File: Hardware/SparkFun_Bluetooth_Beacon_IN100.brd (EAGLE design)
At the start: 25.4 x 25.4 mm, 43 parts, among them J3 Vertical Qwiic Connector, U1 IN100, Y1 CRYSTAL-26MHZSMD-3.2X2.5

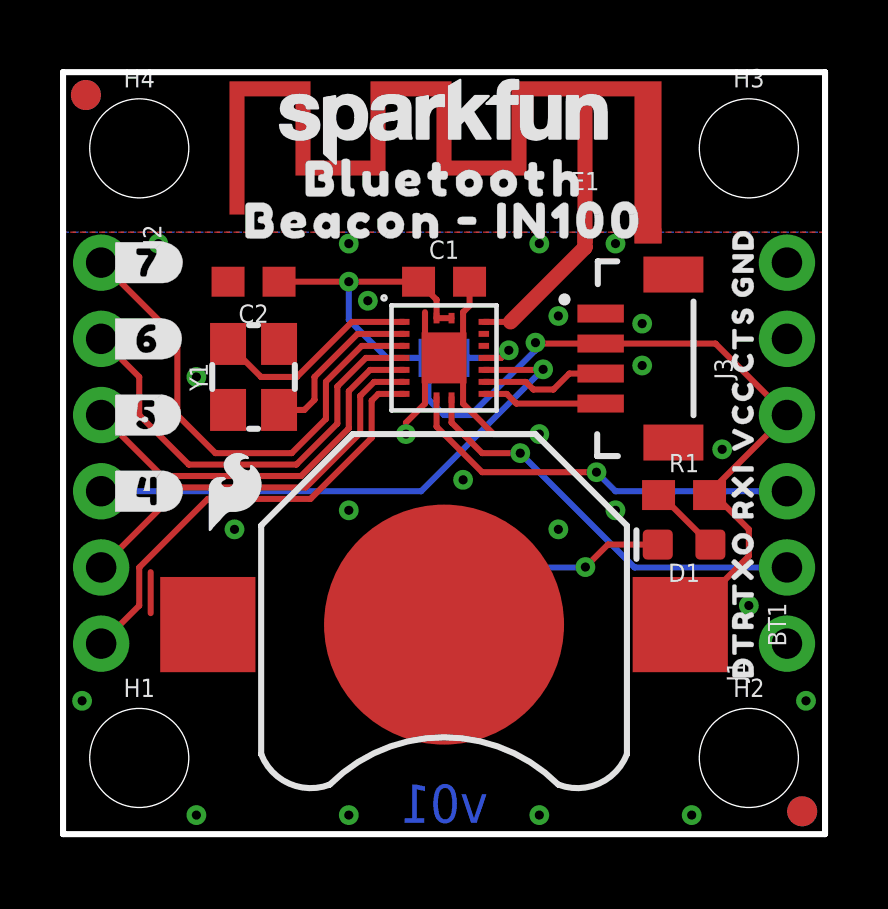
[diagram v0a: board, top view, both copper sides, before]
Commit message: Pre-review cleanup
Clean up schematic
Add "programmed" checkbox to bottom silk
Add SW0 and SW1 to top silk
Update measures
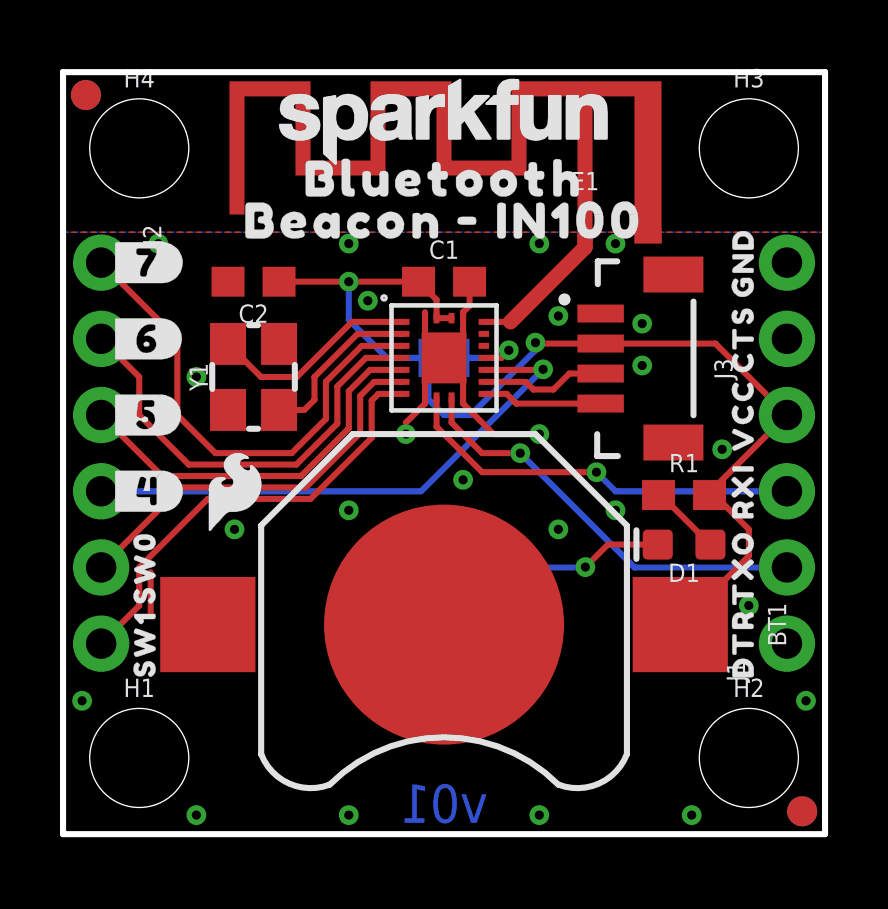
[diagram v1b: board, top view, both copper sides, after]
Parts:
- added U$20: (no value), output:#PROGRAMMED#0
- added U$21: (no value), output:SW00
- added U$22: (no value), output:SW10
- moved FRAME1 8.52 mm to (-10.2, -21.6)
- moved LOGO1 7.62 mm to (12.7, 11.4)
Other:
- board text added: "Dryw Wade"
- board text added: "Units: inches"
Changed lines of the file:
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@@
 </polygon>
 <text x="12.7" y="1.016" size="1.27" layer="16" font="vector" ratio="15" rot="SMR0" align="center">v01</text>
-<dimension x1="0" y1="0" x2="25.4" y2="0" x3="12.7" y3="-3.81" textsize="1.778" textratio="15" layer="47" unit="inch"/>
-<dimension x1="0" y1="0" x2="0" y2="25.4" x3="-1.27" y3="12.7" textsize="1.778" textratio="15" layer="47" unit="inch"/>
+<wire x1="7.62" y1="4.4196" x2="6.35" y2="4.4196" width="0.1524" layer="22"/>
+<wire x1="6.35" y1="4.4196" x2="6.35" y2="3.2004" width="0.1524" layer="22"/>
+<wire x1="6.35" y1="3.2004" x2="7.62" y2="3.2004" width="0.1524" layer="22"/>
+<text x="16.51" y="-21.59" size="1.778" layer="51">Dryw Wade</text>
+<dimension x1="0" y1="0" x2="2.54" y2="0" x3="1.27" y3="-3.81" textsize="1.778" textratio="15" layer="47" unit="inch"/>
+<dimension x1="0" y1="0" x2="22.86" y2="0" x3="11.43" y3="-7.62" textsize="1.778" textratio="15" layer="47" unit="inch"/>
+<dimension x1="0" y1="0" x2="25.4" y2="0" x3="12.7" y3="-11.43" textsize="1.778" textratio="15" layer="47" unit="inch"/>
+<dimension x1="0" y1="0" x2="0" y2="6.35" x3="-1.27" y3="3.175" textsize="1.778" textratio="15" layer="47" unit="inch"/>
+<dimension x1="0" y1="0" x2="0" y2="2.54" x3="-5.08" y3="1.27" textsize="1.778" textratio="15" layer="47" unit="inch"/>
+<dimension x1="0" y1="0" x2="0" y2="19.05" x3="-8.89" y3="9.525" textsize="1.778" textratio="15" layer="47" unit="inch"/>
+<dimension x1="0" y1="0" x2="0" y2="22.86" x3="-12.7" y3="11.43" textsize="1.778" textratio="15" layer="47" unit="inch"/>
+<dimension x1="0" y1="0" x2="0" y2="25.4" x3="-16.51" y3="12.7" textsize="1.778" textratio="15" layer="47" unit="inch"/>
+<text x="-15.24" y="-7.62" size="1.778" layer="47" font="vector" ratio="15">Units: inches</text>
 </plain>
 <attributes>
@@
 <attribute name="VALUE" x="17.399" y="21.209" size="0.6096" layer="27" font="vector" ratio="20" align="top-center"/>
 </element>
-<element name="FRAME1" library="SparkFun-Aesthetics" package="CREATIVE_COMMONS" value="FRAME-LETTER" x="-13.97" y="-13.97" smashed="yes">
-<attribute name="DESIGNER" value="" x="-13.97" y="-13.97" size="1.778" layer="27" font="vector" ratio="15" display="off"/>
-<attribute name="REV" value="" x="-13.97" y="-13.97" size="1.778" layer="27" font="vector" ratio="15" display="off"/>
+<element name="FRAME1" library="SparkFun-Aesthetics" package="CREATIVE_COMMONS" value="FRAME-LETTER" x="-10.16" y="-21.59" smashed="yes">
+<attribute name="DESIGNER" value="" x="-10.16" y="-21.59" size="1.778" layer="27" font="vector" ratio="15" display="off"/>
+<attribute name="REV" value="" x="-10.16" y="-21.59" size="1.778" layer="27" font="vector" ratio="15" display="off"/>
 </element>
 <element name="U1" library="IN100" package="IN100" value="IN100" x="12.7" y="15.875" smashed="yes"/>
@@
 <element name="U$7" library="output" package="#_4#0" value="" x="1.397" y="11.43" smashed="yes"/>
 <element name="U$8" library="SparkFun-Aesthetics" package="SFE_LOGO_FLAME_.1" value="" x="5.715" y="11.43" smashed="yes"/>
-<element name="LOGO1" library="SparkFun-Aesthetics" package="OSHW-LOGO-S" value="OSHW-LOGOS" x="12.7" y="3.81" smashed="yes" rot="MR0"/>
+<element name="LOGO1" library="SparkFun-Aesthetics" package="OSHW-LOGO-S" value="OSHW-LOGOS" x="12.7" y="11.43" smashed="yes" rot="MR0"/>
 <element name="LOGO2" library="SparkFun-Aesthetics" package="SFE_LOGO_NAME_FLAME_.1" value="SFE_LOGO_NAME_FLAME.1_INCH" x="12.7" y="21.59" smashed="yes" rot="MR0"/>
 <element name="U$9" library="output" package="BLUETOOTH0" value="" x="12.7" y="19.304" smashed="yes" rot="MR0"/>
@@
 </element>
 <element name="U$19" library="output" package="#PWR#0" value="" x="12.7" y="7.239" smashed="yes" rot="MR0"/>
+<element name="U$20" library="output" package="#PROGRAMMED#0" value="" x="7.239" y="3.81" smashed="yes" rot="MR0"/>
+<element name="U$21" library="output" package="SW00" value="" x="2.7305" y="8.89" smashed="yes" rot="R90"/>
+<element name="U$22" library="output" package="SW10" value="" x="2.7305" y="6.35" smashed="yes" rot="R90"/>
 </elements>
 <signals>

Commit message: Design review updates
Add TX/RX labels to IN100 symbol
Add text to jumpers in schematic
Add VCC range to schematic
Rename PWR jumper in schematic
Increase crystal trace width to 10mil
Add more GND vias near RF trace
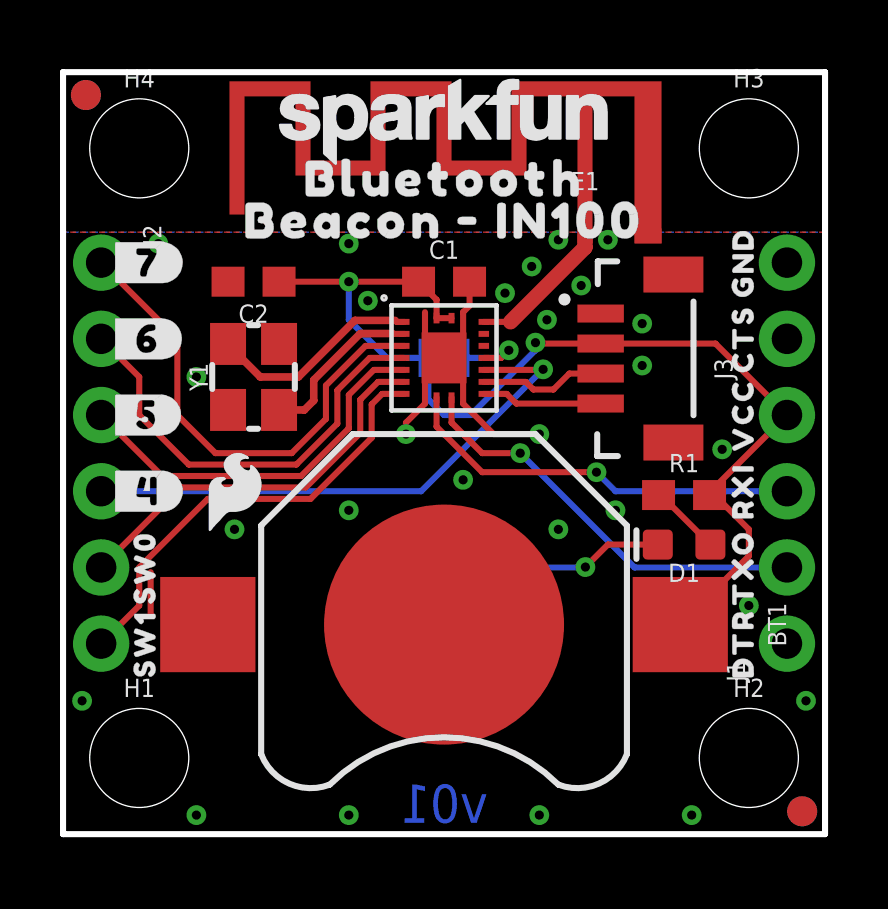
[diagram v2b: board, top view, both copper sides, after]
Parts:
- renumbered VDDQ1 to PWR
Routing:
- net GND: vias 24 -> 27
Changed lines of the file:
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@@
 <drawing>
 <settings>
-<setting alwaysvectorfont="yes"/>
+<setting alwaysvectorfont="no"/>
 <setting verticaltext="up"/>
 </settings>
@@
 <attribute name="VALUE" x="20.701" y="10.541" size="0.6096" layer="27" font="vector" ratio="20" align="top-center"/>
 </element>
-<element name="VDDQ1" library="SparkFun-Jumpers" package="SMT-JUMPER_2_NC_TRACE_SILK" package3d_urn="urn:adsk.eagle:package:39281/1" value="JUMPER-SMT_2_NC_TRACE_SILK" x="12.7" y="8.89" smashed="yes" rot="MR180">
+<element name="PWR" library="SparkFun-Jumpers" package="SMT-JUMPER_2_NC_TRACE_SILK" package3d_urn="urn:adsk.eagle:package:39281/1" value="JUMPER-SMT_2_NC_TRACE_SILK" x="12.7" y="8.89" smashed="yes" rot="MR180">
 <attribute name="NAME" x="12.7" y="7.747" size="0.6096" layer="26" font="vector" ratio="20" rot="MR180" align="bottom-center"/>
 <attribute name="VALUE" x="12.7" y="10.033" size="0.6096" layer="28" font="vector" ratio="20" rot="MR180" align="top-center"/>
@@
 <wire x1="13.55" y1="17.614" x2="13.335" y2="17.399" width="0.2032" layer="1"/>
 <via x="3.175" y="19.685" extent="1-16" drill="0.3048"/>
-<via x="15.875" y="19.685" extent="1-16" drill="0.3048"/>
+<via x="16.51" y="19.812" extent="1-16" drill="0.3048"/>
 <via x="9.525" y="19.685" extent="1-16" drill="0.3048"/>
-<via x="16.51" y="17.272" extent="1-16" drill="0.3048"/>
+<via x="16.129" y="17.145" extent="1-16" drill="0.3048"/>
 <via x="15.875" y="13.335" extent="1-16" drill="0.3048"/>
 <via x="21.971" y="12.827" extent="1-16" drill="0.3048"/>
@@
 <via x="22.86" y="7.62" extent="1-16" drill="0.3048"/>
 <via x="19.304" y="15.621" extent="1-16" drill="0.3048"/>
-<via x="18.415" y="19.685" extent="1-16" drill="0.3048"/>
+<via x="18.161" y="19.812" extent="1-16" drill="0.3048"/>
 <wire x1="11.43" y1="13.335" x2="11.43" y2="13.716" width="0.2032" layer="1"/>
 <wire x1="11.43" y1="13.716" x2="12.065" y2="14.351" width="0.2032" layer="1"/>
 <wire x1="15.875" y1="13.335" x2="14.351" y2="13.335" width="0.2032" layer="1"/>
 <wire x1="14.351" y1="13.335" x2="13.335" y2="14.351" width="0.2032" layer="1"/>
-<contactref element="VDDQ1" pad="1"/>
+<contactref element="PWR" pad="1"/>
 <via x="16.51" y="10.16" extent="1-16" drill="0.3048"/>
 <via x="19.304" y="17.018" extent="1-16" drill="0.3048"/>
@@
 <via x="13.335" y="11.811" extent="1-16" drill="0.3048"/>
 <via x="9.525" y="10.795" extent="1-16" drill="0.3048"/>
+<via x="14.732" y="18.034" extent="1-16" drill="0.3048"/>
+<via x="17.272" y="18.288" extent="1-16" drill="0.3048"/>
+<via x="15.621" y="18.923" extent="1-16" drill="0.3048"/>
 </signal>
 <signal name="N$4">
@@
 <contactref element="U1" pad="1"/>
 <contactref element="Y1" pad="3"/>
-<wire x1="5.5" y1="16.34" x2="6.6" y2="15.24" width="0.2032" layer="1"/>
-<wire x1="9.63013125" y1="17.075" x2="11.375" y2="17.075" width="0.2032" layer="1"/>
-<wire x1="7.79513125" y1="15.24" x2="9.63013125" y2="17.075" width="0.2032" layer="1"/>
-<wire x1="6.6" y1="15.24" x2="7.79513125" y2="15.24" width="0.2032" layer="1"/>
+<wire x1="6.5746" y1="15.24" x2="5.5" y2="16.3146" width="0.254" layer="1"/>
+<wire x1="5.5" y1="16.34" x2="5.5" y2="16.3146" width="0.254" layer="1"/>
+<wire x1="11.121" y1="17.075" x2="11.375" y2="17.075" width="0.2032" layer="1"/>
+<wire x1="11.121" y1="17.075" x2="11.0702" y2="17.1258" width="0.2032" layer="1"/>
+<wire x1="11.0702" y1="17.1258" x2="9.73173125" y2="17.1258" width="0.254" layer="1"/>
+<wire x1="7.84593125" y1="15.24" x2="9.73173125" y2="17.1258" width="0.254" layer="1"/>
+<wire x1="6.5746" y1="15.24" x2="7.84593125" y2="15.24" width="0.254" layer="1"/>
 </signal>
 <signal name="N$2">
 <contactref element="U1" pad="2"/>
 <contactref element="Y1" pad="1"/>
-<wire x1="11.375" y1="16.675" x2="9.817" y2="16.675" width="0.2032" layer="1"/>
-<wire x1="9.817" y1="16.675" x2="8.382" y2="15.24" width="0.2032" layer="1"/>
-<wire x1="8.382" y1="15.24" x2="8.382" y2="14.478" width="0.2032" layer="1"/>
-<wire x1="8.382" y1="14.478" x2="8.044" y2="14.14" width="0.2032" layer="1"/>
-<wire x1="8.044" y1="14.14" x2="7.2" y2="14.14" width="0.2032" layer="1"/>
+<wire x1="11.375" y1="16.675" x2="10.994" y2="16.675" width="0.2032" layer="1"/>
+<wire x1="10.994" y1="16.675" x2="10.9813" y2="16.6877" width="0.2032" layer="1"/>
+<wire x1="10.9813" y1="16.6877" x2="9.9059" y2="16.6877" width="0.254" layer="1"/>
+<wire x1="9.9059" y1="16.6877" x2="8.3566" y2="15.1384" width="0.254" layer="1"/>
+<wire x1="8.3566" y1="15.1384" x2="8.3566" y2="14.4526" width="0.254" layer="1"/>
+<wire x1="8.3566" y1="14.4526" x2="8.044" y2="14.14" width="0.254" layer="1"/>
+<wire x1="8.044" y1="14.14" x2="7.2" y2="14.14" width="0.254" layer="1"/>
 </signal>
 <signal name="VCC">
@@
 <signal name="SW0">
 <contactref element="U1" pad="6"/>
-<wire x1="11.375" y1="15.075" x2="10.372275" y2="15.075" width="0.2032" layer="1"/>
-<wire x1="10.372275" y1="15.075" x2="9.906" y2="14.608725" width="0.2032" layer="1"/>
+<wire x1="11.375" y1="15.075" x2="10.499275" y2="15.075" width="0.2032" layer="1"/>
+<wire x1="10.499275" y1="15.075" x2="9.906" y2="14.481725" width="0.2032" layer="1"/>
 <wire x1="9.906" y1="13.36954375" x2="8.09345625" y2="11.557" width="0.2032" layer="1"/>
-<wire x1="9.906" y1="14.608725" x2="9.906" y2="13.36954375" width="0.2032" layer="1"/>
+<wire x1="9.906" y1="14.481725" x2="9.906" y2="13.36954375" width="0.2032" layer="1"/>
 <wire x1="8.09345625" y1="11.557" x2="3.937" y2="11.557" width="0.2032" layer="1"/>
 <contactref element="J2" pad="5"/>
@@
 <signal name="SW1">
 <contactref element="U1" pad="7"/>
-<wire x1="11.375" y1="14.675" x2="10.51109375" y2="14.675" width="0.2032" layer="1"/>
-<wire x1="10.287" y1="14.45090625" x2="10.287" y2="13.211725" width="0.2032" layer="1"/>
-<wire x1="10.51109375" y1="14.675" x2="10.287" y2="14.45090625" width="0.2032" layer="1"/>
+<wire x1="11.375" y1="14.675" x2="10.63809375" y2="14.675" width="0.2032" layer="1"/>
+<wire x1="10.287" y1="14.32390625" x2="10.287" y2="13.211725" width="0.2032" layer="1"/>
+<wire x1="10.63809375" y1="14.675" x2="10.287" y2="14.32390625" width="0.2032" layer="1"/>
 <wire x1="10.287" y1="13.211725" x2="8.251275" y2="11.176" width="0.2032" layer="1"/>
 <wire x1="4.826" y1="11.176" x2="2.54" y2="8.89" width="0.2032" layer="1"/>
@@
 <signal name="IO5">
 <contactref element="U1" pad="5"/>
-<wire x1="11.375" y1="15.475" x2="10.23345625" y2="15.475" width="0.2032" layer="1"/>
-<wire x1="10.23345625" y1="15.475" x2="9.525" y2="14.76654375" width="0.2032" layer="1"/>
+<wire x1="11.375" y1="15.475" x2="10.36045625" y2="15.475" width="0.2032" layer="1"/>
+<wire x1="10.36045625" y1="15.475" x2="9.525" y2="14.63954375" width="0.2032" layer="1"/>
 <wire x1="9.525" y1="13.5273625" x2="7.9356375" y2="11.938" width="0.2032" layer="1"/>
-<wire x1="9.525" y1="14.76654375" x2="9.525" y2="13.5273625" width="0.2032" layer="1"/>
+<wire x1="9.525" y1="14.63954375" x2="9.525" y2="13.5273625" width="0.2032" layer="1"/>
 <wire x1="3.302" y1="11.938" x2="7.9356375" y2="11.938" width="0.2032" layer="1"/>
 <contactref element="J2" pad="3"/>
@@
 <signal name="IO6">
 <contactref element="U1" pad="4"/>
-<wire x1="11.375" y1="15.875" x2="10.0946375" y2="15.875" width="0.2032" layer="1"/>
-<wire x1="10.0946375" y1="15.875" x2="9.144" y2="14.9243625" width="0.2032" layer="1"/>
+<wire x1="11.375" y1="15.875" x2="10.2216375" y2="15.875" width="0.2032" layer="1"/>
+<wire x1="10.2216375" y1="15.875" x2="9.144" y2="14.7973625" width="0.2032" layer="1"/>
 <wire x1="9.144" y1="13.68518125" x2="7.77781875" y2="12.319" width="0.2032" layer="1"/>
-<wire x1="9.144" y1="14.9243625" x2="9.144" y2="13.68518125" width="0.2032" layer="1"/>
+<wire x1="9.144" y1="14.7973625" x2="9.144" y2="13.68518125" width="0.2032" layer="1"/>
 <wire x1="2.54" y1="13.97" x2="2.54" y2="15.24" width="0.2032" layer="1"/>
 <wire x1="7.77781875" y1="12.319" x2="4.191" y2="12.319" width="0.2032" layer="1"/>
@@
 <signal name="IO7">
 <contactref element="U1" pad="3"/>
-<wire x1="11.375" y1="16.275" x2="9.95581875" y2="16.275" width="0.2032" layer="1"/>
-<wire x1="9.95581875" y1="16.275" x2="8.763" y2="15.08218125" width="0.2032" layer="1"/>
+<wire x1="11.375" y1="16.275" x2="10.08281875" y2="16.275" width="0.2032" layer="1"/>
+<wire x1="10.08281875" y1="16.275" x2="8.763" y2="14.95518125" width="0.2032" layer="1"/>
 <wire x1="8.763" y1="13.843" x2="7.62" y2="12.7" width="0.2032" layer="1"/>
-<wire x1="8.763" y1="15.08218125" x2="8.763" y2="13.843" width="0.2032" layer="1"/>
+<wire x1="8.763" y1="14.95518125" x2="8.763" y2="13.843" width="0.2032" layer="1"/>
 <wire x1="5.08" y1="12.7" x2="3.81" y2="13.97" width="0.2032" layer="1"/>
 <wire x1="3.81" y1="13.97" x2="3.81" y2="16.51" width="0.2032" layer="1"/>
@@
 </signal>
 <signal name="N$5">
-<contactref element="VDDQ1" pad="2"/>
+<contactref element="PWR" pad="2"/>
 <contactref element="D1" pad="C"/>
 <wire x1="19.824" y1="9.652" x2="18.161" y2="9.652" width="0.2032" layer="1"/>

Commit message: Design review updates
Update serial connector silk on back side
Change "Programmed" checkbox to "Board info" silk region for general notes
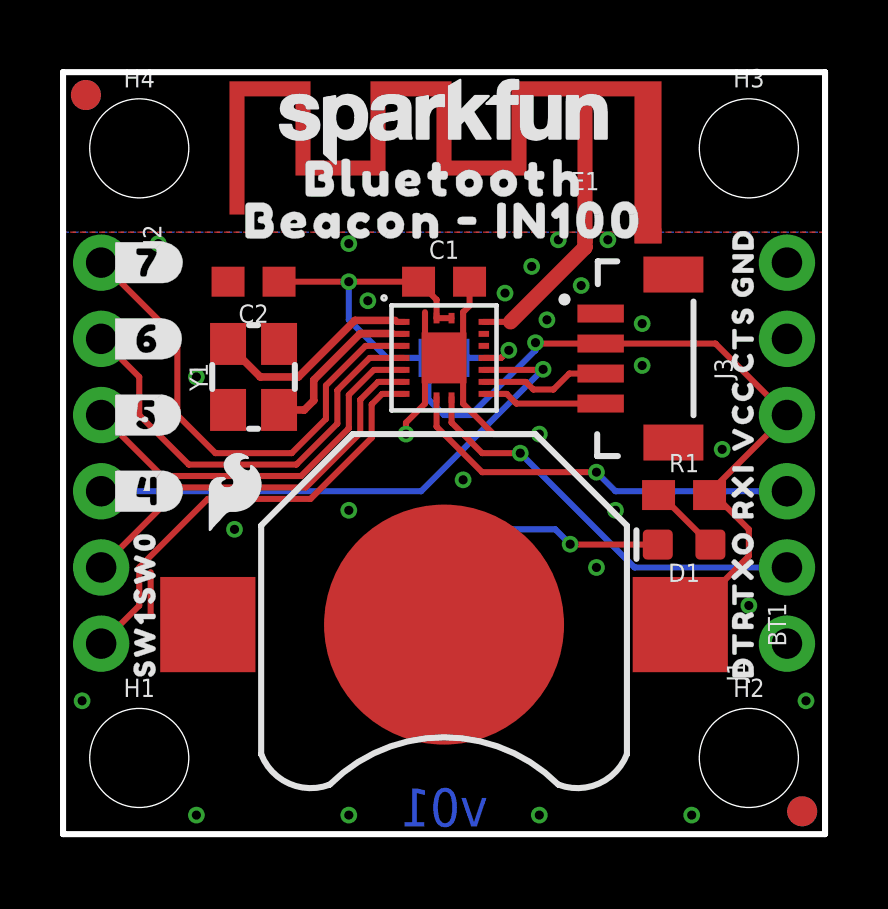
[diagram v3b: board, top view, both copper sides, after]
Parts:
- removed U$20: (no value), output:#PROGRAMMED#0
- added U$23: (no value), output:#BOARD_INFO#0
- moved LOGO1 5.24 mm to (7.62, 12.7)
- moved U$19 4.57 mm to (12.7, 11.8)
- moved PWR 1.27 mm to (12.7, 10.2)
- moved U$12 1.27 mm to (19.7, 12.7)
